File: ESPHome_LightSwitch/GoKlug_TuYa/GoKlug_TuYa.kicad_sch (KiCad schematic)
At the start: 29 parts

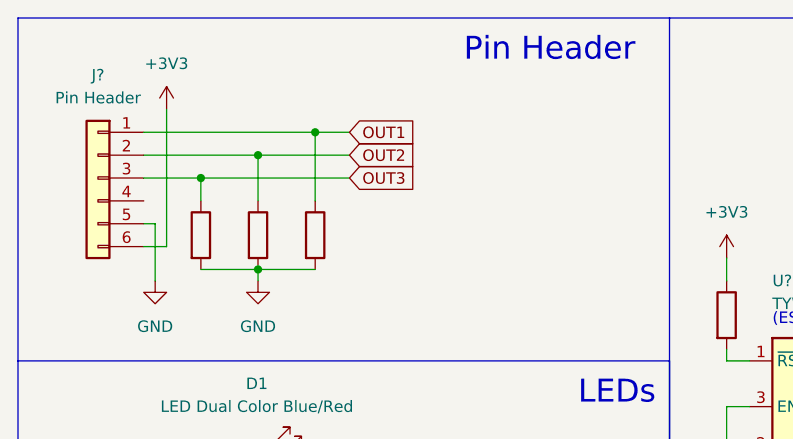
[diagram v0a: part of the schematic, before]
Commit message: Added fix to schematic and added esphome config file
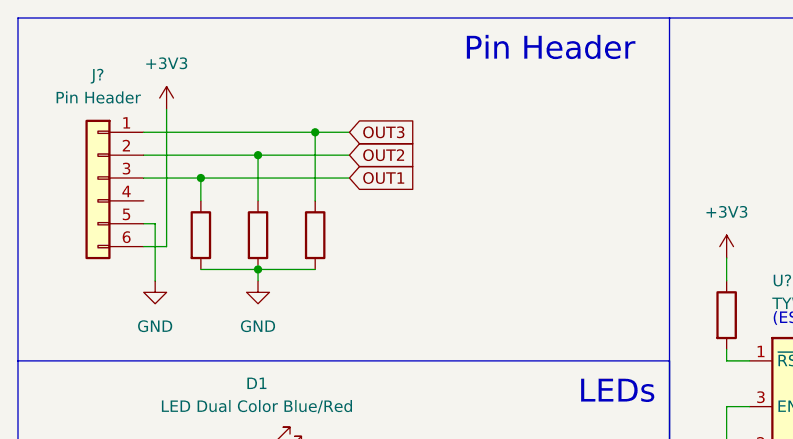
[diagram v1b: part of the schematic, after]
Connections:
- net OUT1: now also J?.3 (Pin_3), R?.1; no longer J?.1 (Pin_1), R?.1
- net OUT3: now also J?.1 (Pin_1), R?.1; no longer J?.3 (Pin_3), R?.1
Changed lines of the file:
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@@
     )
   )
-  (global_label "OUT3" (shape input) (at 49.53 30.48 0) (fields_autoplaced)
+  (global_label "OUT1" (shape input) (at 49.53 30.48 0) (fields_autoplaced)
     (effects (font (size 1.27 1.27)) (justify left))
     (property "Intersheet References" "${INTERSHEET_REFS}" (id 0) (at 56.7812 30.4006 0)
@@
     )
   )
-  (global_label "OUT1" (shape input) (at 49.53 25.4 0) (fields_autoplaced)
+  (global_label "OUT3" (shape input) (at 49.53 25.4 0) (fields_autoplaced)
     (effects (font (size 1.27 1.27)) (justify left))
     (property "Intersheet References" "${INTERSHEET_REFS}" (id 0) (at 56.7812 25.3206 0)
